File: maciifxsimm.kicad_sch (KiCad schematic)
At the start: 11 parts, among them J1 SIMM64_EDGE, U1 KM41C16000CK, U2 KM41C16000CK, U3 KM41C16000CK, U4 KM41C16000CK, U5 KM41C16000CK, U6 KM41C16000CK, U7 KM41C16000CK, U8 KM41C16000CK

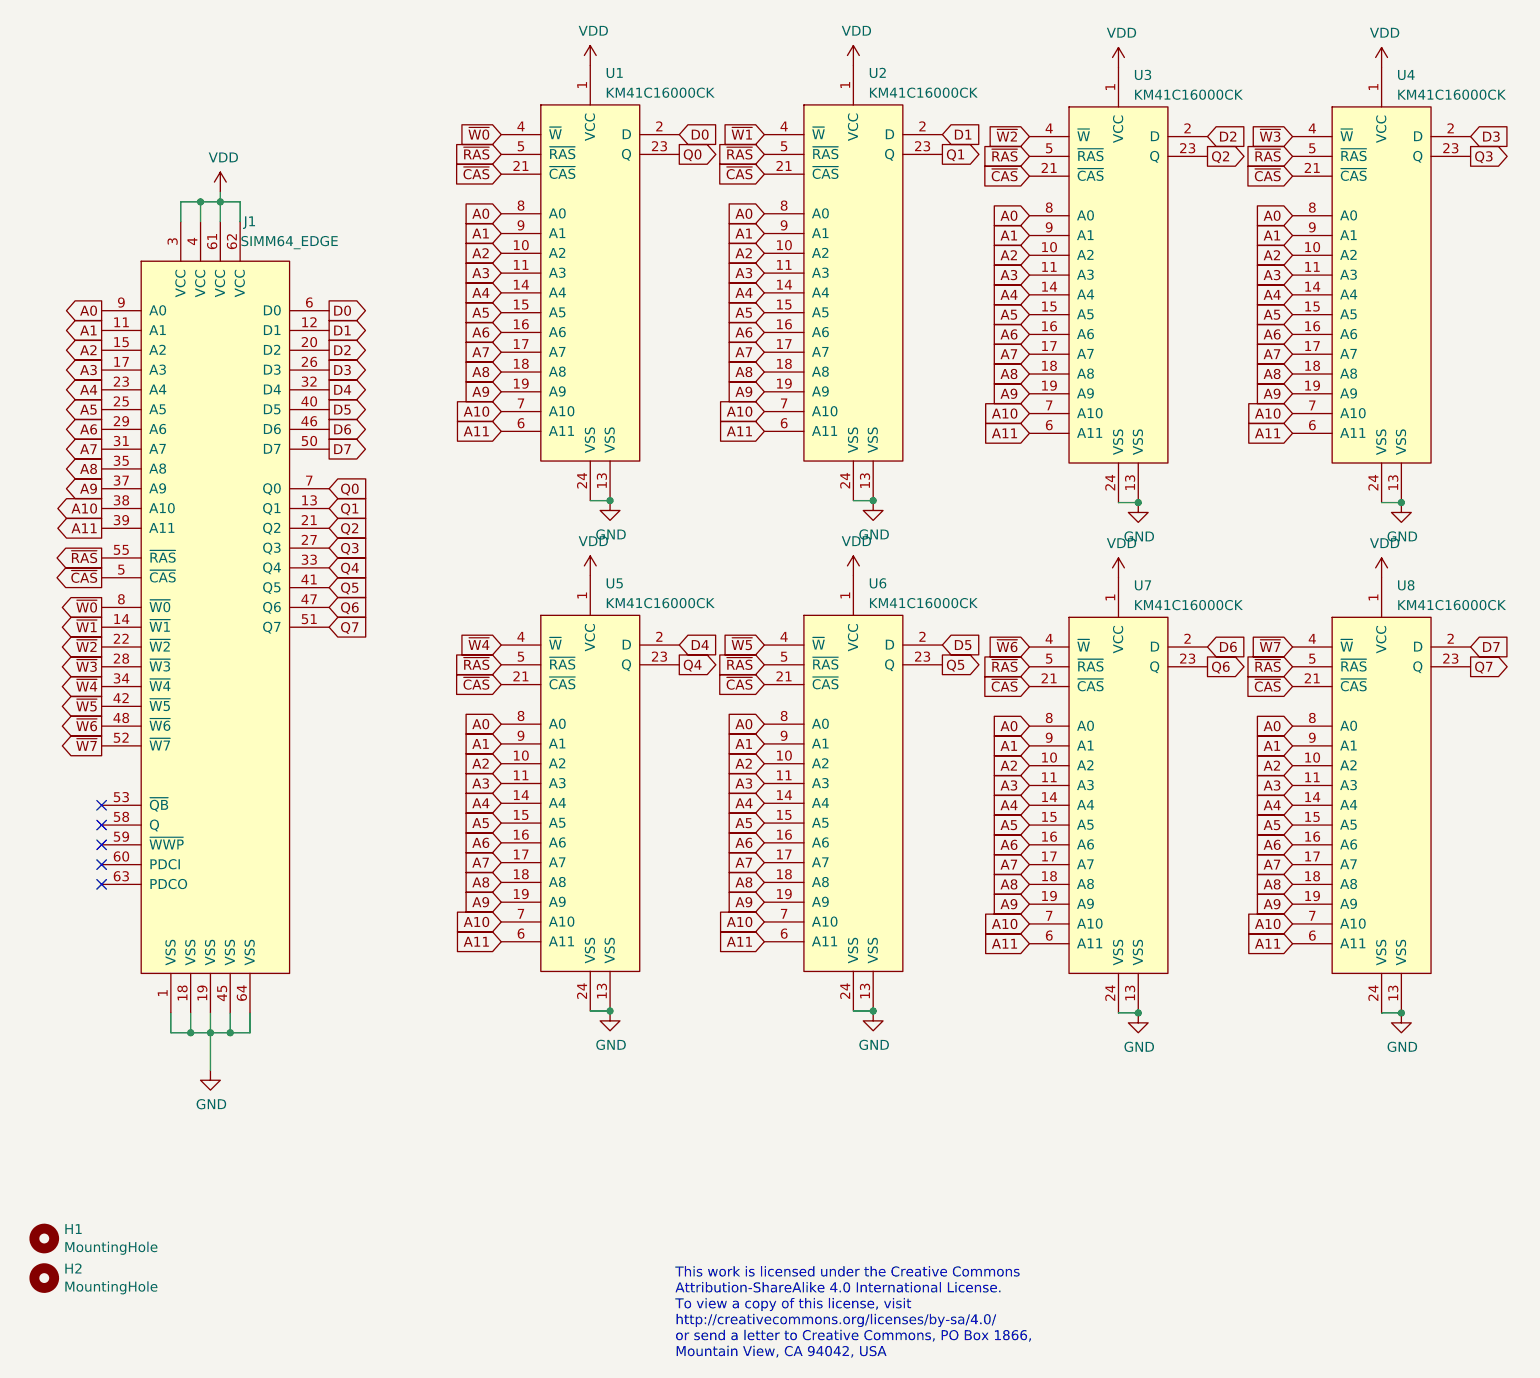
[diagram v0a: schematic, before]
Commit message: fix issues found in the first run
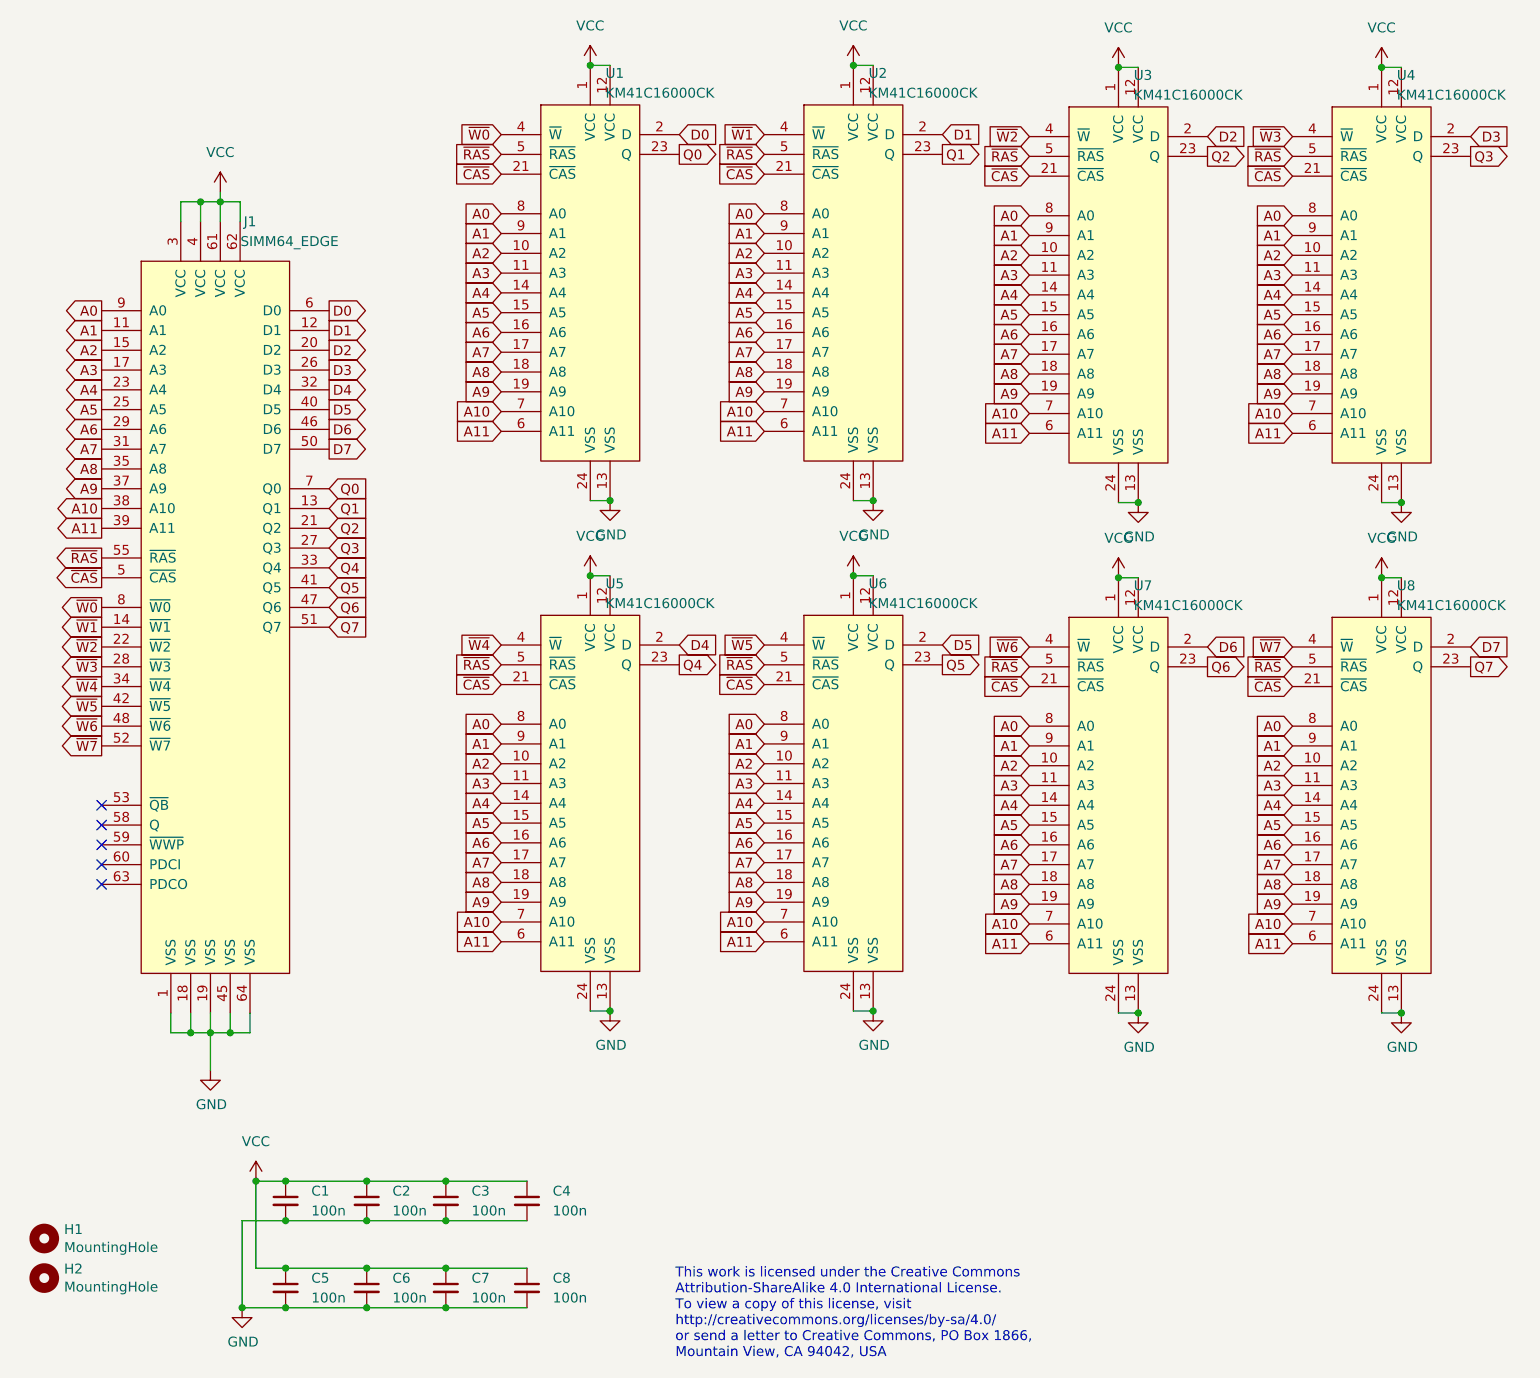
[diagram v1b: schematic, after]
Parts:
- added C1, C2, C3, C4, C5, C6, C7, C8: 100n, Capacitor_SMD:C_0603_1608Metric_Pad1.08x0.95mm_HandSolder, symbol Device:C_Small
- U1, U2, U3, U4, U5, U6, U7, U8: footprint hans-kicad-footprints:SOJ-24-26 -> Active:SOJ127P851X356-20_alt
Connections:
- net GND: now also C1.2, C2.2, C3.2, C4.2, C5.2, C6.2, C7.2, C8.2
- net VDD renamed VCC
- net VCC: now also U1.12 (VCC), U2.12 (VCC), U3.12 (VCC), U4.12 (VCC), U5.12 (VCC), U6.12 (VCC), U7.12 (VCC), U8.12 (VCC), C1.1, C2.1, C3.1, C4.1, C5.1, C6.1, C7.1, C8.1
